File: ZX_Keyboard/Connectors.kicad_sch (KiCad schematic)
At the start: 18 parts

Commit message: update keyboard pcb
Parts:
- JC1: value USB_A -> USB
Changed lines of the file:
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@@
   (symbol (lib_id "power:VCC") (at 114.3 76.2 90) (unit 1)
     (in_bom yes) (on_board yes) (fields_autoplaced)
-    (property "Reference" "#PWR032" (id 0) (at 118.11 76.2 0)
+    (property "Reference" "#PWR034" (id 0) (at 118.11 76.2 0)
       (effects (font (size 1.27 1.27)) hide)
     )
@@
       (effects (font (size 1.27 1.27)) (justify right))
     )
-    (property "Value" "USB_A" (id 1) (at 267.97 116.8399 0)
+    (property "Value" "USB" (id 1) (at 267.97 116.8399 0)
       (effects (font (size 1.27 1.27)) (justify right))
     )
@@
   (symbol (lib_id "power:GND") (at 114.3 68.58 270) (unit 1)
     (in_bom yes) (on_board yes)
-    (property "Reference" "#PWR029" (id 0) (at 107.95 68.58 0)
+    (property "Reference" "#PWR031" (id 0) (at 107.95 68.58 0)
       (effects (font (size 1.27 1.27)) hide)
     )
@@
   (symbol (lib_id "power:GND") (at 261.62 130.81 0) (unit 1)
     (in_bom yes) (on_board yes) (fields_autoplaced)
-    (property "Reference" "#PWR036" (id 0) (at 261.62 137.16 0)
+    (property "Reference" "#PWR038" (id 0) (at 261.62 137.16 0)
       (effects (font (size 1.27 1.27)) hide)
     )
@@
   (symbol (lib_id "power:GND") (at 151.13 120.65 0) (unit 1)
     (in_bom yes) (on_board yes) (fields_autoplaced)
-    (property "Reference" "#PWR035" (id 0) (at 151.13 127 0)
+    (property "Reference" "#PWR037" (id 0) (at 151.13 127 0)
       (effects (font (size 1.27 1.27)) hide)
     )
@@
   (symbol (lib_id "power:GND") (at 125.73 101.6 0) (unit 1)
     (in_bom yes) (on_board yes) (fields_autoplaced)
-    (property "Reference" "#PWR033" (id 0) (at 125.73 107.95 0)
+    (property "Reference" "#PWR035" (id 0) (at 125.73 107.95 0)
       (effects (font (size 1.27 1.27)) hide)
     )
@@
   (symbol (lib_id "power:GND") (at 76.2 187.96 0) (unit 1)
     (in_bom yes) (on_board yes) (fields_autoplaced)
-    (property "Reference" "#PWR037" (id 0) (at 76.2 194.31 0)
+    (property "Reference" "#PWR039" (id 0) (at 76.2 194.31 0)
       (effects (font (size 1.27 1.27)) hide)
     )
@@
   (symbol (lib_id "power:VCC") (at 232.41 31.75 0) (unit 1)
     (in_bom yes) (on_board yes) (fields_autoplaced)
-    (property "Reference" "#PWR0102" (id 0) (at 232.41 35.56 0)
+    (property "Reference" "#PWR029" (id 0) (at 232.41 35.56 0)
       (effects (font (size 1.27 1.27)) hide)
     )
@@
   (symbol (lib_id "power:+3.3V") (at 114.3 60.96 90) (unit 1)
     (in_bom yes) (on_board yes)
-    (property "Reference" "#PWR028" (id 0) (at 118.11 60.96 0)
+    (property "Reference" "#PWR030" (id 0) (at 118.11 60.96 0)
       (effects (font (size 1.27 1.27)) hide)
     )
@@
   (symbol (lib_id "power:GND") (at 188.595 101.6 0) (unit 1)
     (in_bom yes) (on_board yes) (fields_autoplaced)
-    (property "Reference" "#PWR034" (id 0) (at 188.595 107.95 0)
+    (property "Reference" "#PWR036" (id 0) (at 188.595 107.95 0)
       (effects (font (size 1.27 1.27)) hide)
     )
@@
   (symbol (lib_id "power:GND") (at 222.25 72.39 0) (unit 1)
     (in_bom yes) (on_board yes)
-    (property "Reference" "#PWR030" (id 0) (at 222.25 78.74 0)
+    (property "Reference" "#PWR032" (id 0) (at 222.25 78.74 0)
       (effects (font (size 1.27 1.27)) hide)
     )
@@
   (symbol (lib_id "power:GND") (at 232.41 72.39 0) (unit 1)
     (in_bom yes) (on_board yes)
-    (property "Reference" "#PWR031" (id 0) (at 232.41 78.74 0)
-      (effects (font (size 1.27 1.27)) hide)
-    )
+    (property "Reference" "#PWR033" (id 0) (at 232.41 78.74 0)
+      (effects (font (size 1.27 1.27)) hide)
+    )

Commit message: teracing and refactoring connectors
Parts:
- removed JC2: ZX_Date, Connector_PinHeader_2.54mm:PinHeader_1x05_P2.54mm_Vertical, symbol Connector_Generic:Conn_01x05
- added JC2: ZX_Date, Connector_PinHeader_2.54mm:PinHeader_1x07_P2.54mm_Vertical, symbol Connector_Generic:Conn_01x07
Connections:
- net GND: now also JC2.7 (Pin_7)
- net IN: no longer JC3.2 (Pin_2)
- net KeyD0: now also JC2.1 (Pin_1)
- net KeyD1: now also JC2.2 (Pin_2)
- net KeyD2: now also JC2.3 (Pin_3)
- net KeyD3: now also JC2.4 (Pin_4)
- net KeyD4: now also JC2.5 (Pin_5)
- net VIN+5V: now also JC3.2 (Pin_2), JC2.6 (Pin_6)
- net USB_OTG_FS_DM- renamed USB_OTG_FS_DM
- net USB_OTG_FS_DP+ renamed USB_OTG_FS_DP
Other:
- moved on the sheet: CC1, CC2, JC1, JC3, JC4, JC5, LEDC1, LEDC2, QC1, RC1, RC2, RC3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

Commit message: update pcb
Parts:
- renumbered JC3 to JC2, JC2 to JC3, RC4 to RC2, RC5 to RC3, RC2 to RC4, RC3 to RC5
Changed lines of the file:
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@@
   (symbol (lib_id "power:VCC") (at 113.03 50.8 90) (unit 1)
     (in_bom yes) (on_board yes) (fields_autoplaced)
-    (property "Reference" "#PWR034" (id 0) (at 116.84 50.8 0)
+    (property "Reference" "#PWR035" (id 0) (at 116.84 50.8 0)
       (effects (font (size 1.27 1.27)) hide)
     )
@@
   (symbol (lib_id "Device:R") (at 149.86 46.99 0) (unit 1)
     (in_bom yes) (on_board yes) (fields_autoplaced)
-    (property "Reference" "RC5" (id 0) (at 152.4 45.7199 0)
+    (property "Reference" "RC3" (id 0) (at 152.4 45.7199 0)
       (effects (font (size 1.27 1.27)) (justify left))
     )
@@
   (symbol (lib_id "Connector_Generic:Conn_01x07") (at 26.67 143.51 0) (mirror y) (unit 1)
     (in_bom yes) (on_board yes)
-    (property "Reference" "JC2" (id 0) (at 26.67 133.35 0))
+    (property "Reference" "JC3" (id 0) (at 26.67 133.35 0))
     (property "Value" "ZX_Date" (id 1) (at 26.67 153.67 0))
     (property "Footprint" "Connector_PinHeader_2.54mm:PinHeader_1x07_P2.54mm_Vertical" (id 2) (at 26.67 143.51 0)
@@
   (symbol (lib_id "Connector_Generic:Conn_02x09_Odd_Even") (at 90.17 140.97 0) (unit 1)
     (in_bom yes) (on_board yes)
-    (property "Reference" "JC3" (id 0) (at 91.44 124.46 0))
+    (property "Reference" "JC2" (id 0) (at 91.44 124.46 0))
     (property "Value" "General_Keyboard 8x8" (id 1) (at 90.17 153.67 0))
     (property "Footprint" "Connector_PinHeader_2.54mm:PinHeader_2x09_P2.54mm_Vertical" (id 2) (at 90.17 140.97 0)
@@
   (symbol (lib_id "Device:R") (at 214.63 50.8 90) (unit 1)
     (in_bom yes) (on_board yes)
-    (property "Reference" "RC2" (id 0) (at 214.63 48.26 90))
+    (property "Reference" "RC4" (id 0) (at 214.63 48.26 90))
     (property "Value" "47kOm" (id 1) (at 214.63 53.34 90))
     (property "Footprint" "Resistor_SMD:R_0805_2012Metric_Pad1.20x1.40mm_HandSolder" (id 2) (at 214.63 52.578 90)
@@
   (symbol (lib_id "Device:R") (at 220.98 57.15 0) (unit 1)
     (in_bom yes) (on_board yes)
-    (property "Reference" "RC3" (id 0) (at 223.52 54.61 0))
+    (property "Reference" "RC5" (id 0) (at 223.52 54.61 0))
     (property "Value" "22kOm" (id 1) (at 226.06 59.69 0))
     (property "Footprint" "Resistor_SMD:R_0805_2012Metric_Pad1.20x1.40mm_HandSolder" (id 2) (at 219.202 57.15 90)
@@
   (symbol (lib_id "power:GND") (at 113.03 43.18 270) (unit 1)
     (in_bom yes) (on_board yes)
-    (property "Reference" "#PWR031" (id 0) (at 106.68 43.18 0)
+    (property "Reference" "#PWR034" (id 0) (at 106.68 43.18 0)
       (effects (font (size 1.27 1.27)) hide)
     )
@@
   (symbol (lib_id "power:GND") (at 260.35 105.41 0) (unit 1)
     (in_bom yes) (on_board yes) (fields_autoplaced)
-    (property "Reference" "#PWR038" (id 0) (at 260.35 111.76 0)
+    (property "Reference" "#PWR041" (id 0) (at 260.35 111.76 0)
       (effects (font (size 1.27 1.27)) hide)
     )
@@
   (symbol (lib_id "power:GND") (at 149.86 95.25 0) (unit 1)
     (in_bom yes) (on_board yes) (fields_autoplaced)
-    (property "Reference" "#PWR037" (id 0) (at 149.86 101.6 0)
+    (property "Reference" "#PWR040" (id 0) (at 149.86 101.6 0)
       (effects (font (size 1.27 1.27)) hide)
     )
@@
   (symbol (lib_id "power:GND") (at 124.46 76.2 0) (unit 1)
     (in_bom yes) (on_board yes)
-    (property "Reference" "#PWR035" (id 0) (at 124.46 82.55 0)
+    (property "Reference" "#PWR038" (id 0) (at 124.46 82.55 0)
       (effects (font (size 1.27 1.27)) hide)
     )
@@
   (symbol (lib_id "Device:R") (at 161.29 41.91 0) (unit 1)
     (in_bom yes) (on_board yes) (fields_autoplaced)
-    (property "Reference" "RC4" (id 0) (at 163.83 40.6399 0)
+    (property "Reference" "RC2" (id 0) (at 163.83 40.6399 0)
       (effects (font (size 1.27 1.27)) (justify left))
     )
@@
   (symbol (lib_id "power:GND") (at 77.47 153.67 0) (unit 1)
     (in_bom yes) (on_board yes) (fields_autoplaced)
-    (property "Reference" "#PWR039" (id 0) (at 77.47 160.02 0)
+    (property "Reference" "#PWR043" (id 0) (at 77.47 160.02 0)
       (effects (font (size 1.27 1.27)) hide)
     )
@@
   (symbol (lib_id "power:VCC") (at 231.14 22.86 0) (unit 1)
     (in_bom yes) (on_board yes) (fields_autoplaced)
-    (property "Reference" "#PWR029" (id 0) (at 231.14 26.67 0)
+    (property "Reference" "#PWR032" (id 0) (at 231.14 26.67 0)
       (effects (font (size 1.27 1.27)) hide)
     )
@@
   (symbol (lib_id "power:GND") (at 35.56 153.67 0) (mirror y) (unit 1)
     (in_bom yes) (on_board yes) (fields_autoplaced)
-    (property "Reference" "#PWR0104" (id 0) (at 35.56 160.02 0)
+    (property "Reference" "#PWR042" (id 0) (at 35.56 160.02 0)
       (effects (font (size 1.27 1.27)) hide)
     )
@@
   (symbol (lib_id "power:+3.3V") (at 113.03 35.56 90) (unit 1)
     (in_bom yes) (on_board yes)
-    (property "Reference" "#PWR030" (id 0) (at 116.84 35.56 0)
+    (property "Reference" "#PWR033" (id 0) (at 116.84 35.56 0)
       (effects (font (size 1.27 1.27)) hide)
     )
@@
   (symbol (lib_id "power:GND") (at 187.325 76.2 0) (unit 1)
     (in_bom yes) (on_board yes) (fields_autoplaced)
-    (property "Reference" "#PWR036" (id 0) (at 187.325 82.55 0)
+    (property "Reference" "#PWR039" (id 0) (at 187.325 82.55 0)
       (effects (font (size 1.27 1.27)) hide)
     )
@@
   (symbol (lib_id "power:GND") (at 220.98 63.5 0) (unit 1)
     (in_bom yes) (on_board yes)
-    (property "Reference" "#PWR032" (id 0) (at 220.98 69.85 0)
+    (property "Reference" "#PWR036" (id 0) (at 220.98 69.85 0)
       (effects (font (size 1.27 1.27)) hide)
     )
@@
   (symbol (lib_id "power:GND") (at 231.14 63.5 0) (unit 1)
     (in_bom yes) (on_board yes)
-    (property "Reference" "#PWR033" (id 0) (at 231.14 69.85 0)
-      (effects (font (size 1.27 1.27)) hide)
-    )
+    (property "Reference" "#PWR037" (id 0) (at 231.14 69.85 0)
+      (effects (font (size 1.27 1.27)) hide)
+    )

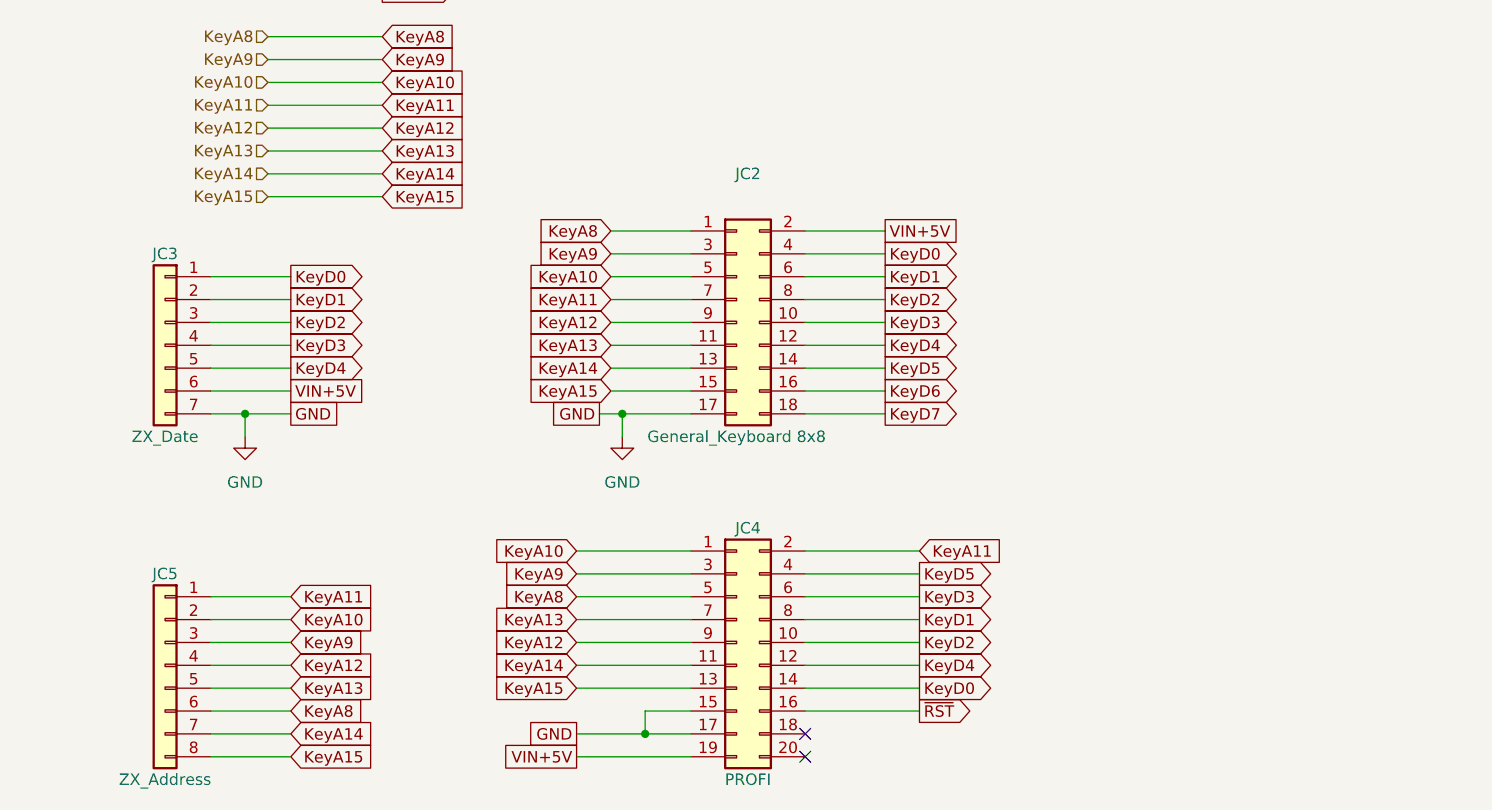
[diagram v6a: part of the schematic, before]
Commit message: update keyboard connection
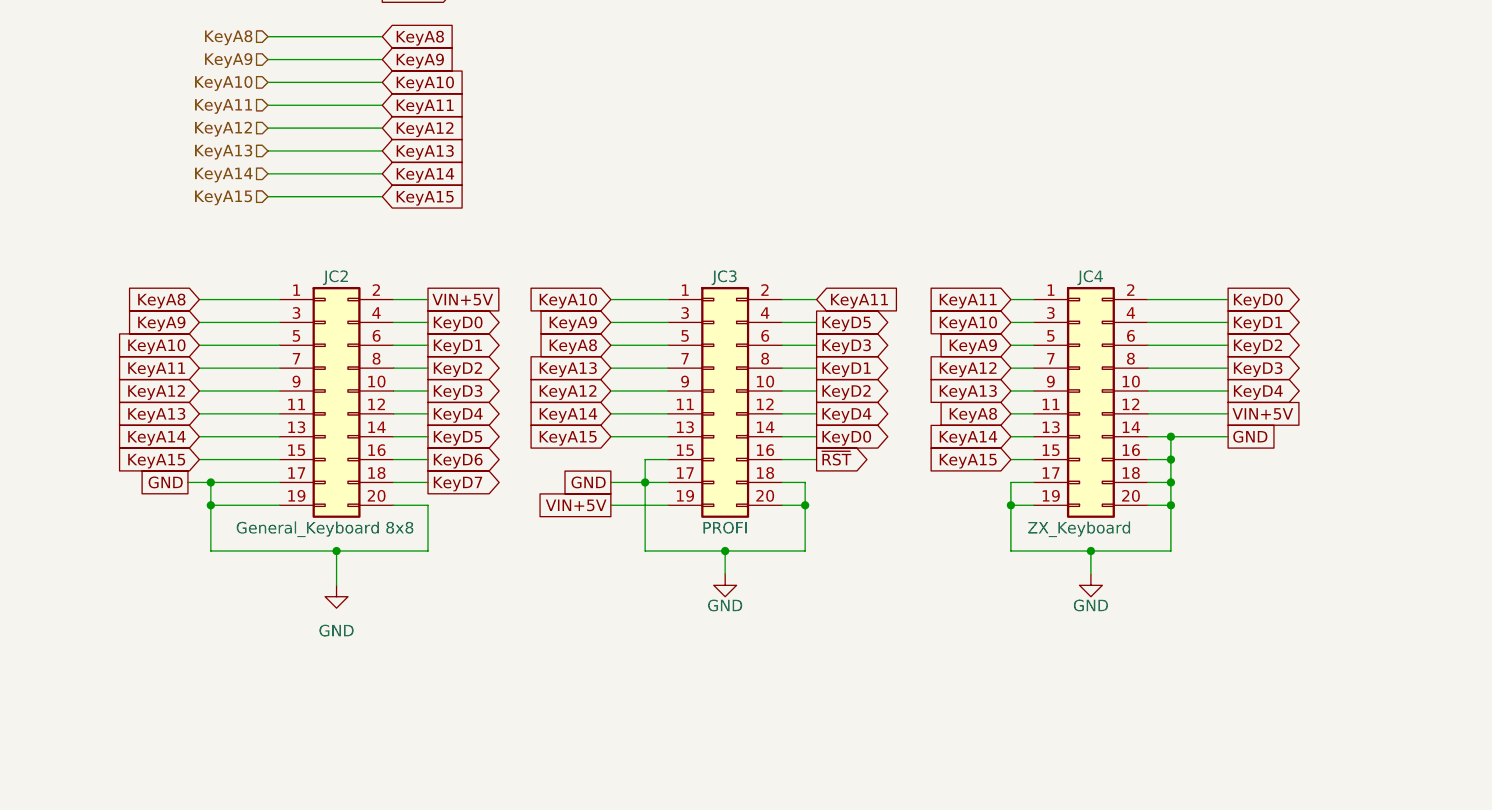
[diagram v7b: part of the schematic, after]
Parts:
- removed JC3: ZX_Date, Connector_PinHeader_2.54mm:PinHeader_1x07_P2.54mm_Vertical, symbol Connector_Generic:Conn_01x07
- removed JC5: ZX_Address, Connector_PinHeader_2.54mm:PinHeader_1x08_P2.54mm_Vertical, symbol Connector_Generic:Conn_01x08
- added JC4: ZX_Keyboard, Connector_PinHeader_2.54mm:PinHeader_2x10_P2.54mm_Vertical, symbol Connector_Generic:Conn_02x10_Odd_Even
- JC2: footprint Connector_PinHeader_2.54mm:PinHeader_2x09_P2.54mm_Vertical -> Connector_PinHeader_2.54mm:PinHeader_2x10_P2.54mm_Vertical; symbol Connector_Generic:Conn_02x09_Odd_Even -> Connector_Generic:Conn_02x10_Odd_Even
- renumbered JC4 to JC3
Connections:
- net GND: now also JC2.19 (Pin_19), JC2.20 (Pin_20), JC3.18 (Pin_18), JC3.20 (Pin_20), JC4.14 (Pin_14), JC4.16 (Pin_16), JC4.17 (Pin_17), JC4.18 (Pin_18), JC4.19 (Pin_19), JC4.20 (Pin_20)
- net KeyA10: now also JC4.3 (Pin_3)
- net KeyA11: now also JC4.1 (Pin_1)
- net KeyA12: now also JC4.7 (Pin_7)
- net KeyA13: now also JC4.9 (Pin_9)
- net KeyA14: now also JC4.13 (Pin_13)
- net KeyA15: now also JC4.15 (Pin_15)
- net KeyA8: now also JC4.11 (Pin_11)
- net KeyA9: now also JC4.5 (Pin_5)
- net KeyD0: now also JC4.2 (Pin_2)
- net KeyD1: now also JC4.4 (Pin_4)
- net KeyD2: now also JC4.6 (Pin_6)
- net KeyD3: now also JC4.8 (Pin_8)
- net KeyD4: now also JC4.10 (Pin_10)
- net VIN+5V: now also JC4.12 (Pin_12)
- no-connect marks 2 -> 0
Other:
- moved on the sheet: JC3
